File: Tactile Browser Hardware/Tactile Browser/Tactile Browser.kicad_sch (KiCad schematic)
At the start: 79 parts, among them SW1 SW_Push, SW10 SW_Push, SW11 SW_Push, SW12 SW_Push, SW13 SW_Push, SW14 SW_Push, SW15 SW_Push, SW16 SW_Push, SW17 SW_Push, SW18 SW_Push, SW19 SW_Push, SW2 SW_Push, SW20 SW_Push, SW3 SW_Push, SW4 SW_Push, SW5 SW_Push, SW6 SW_Push, SW7 SW_Push, SW8 SW_Push, SW9 SW_Push

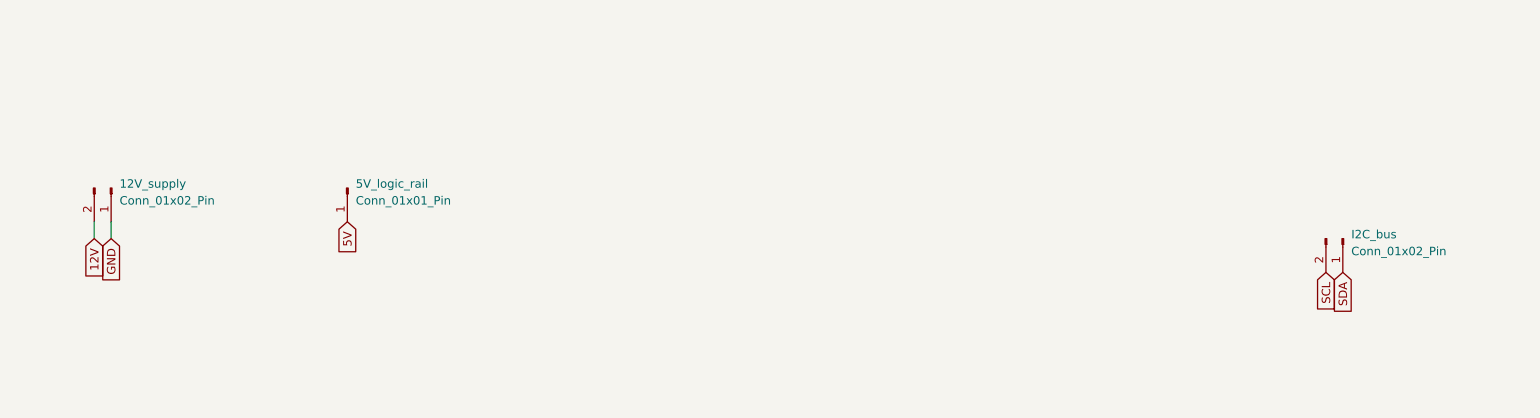
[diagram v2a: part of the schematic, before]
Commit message: added footprints to module
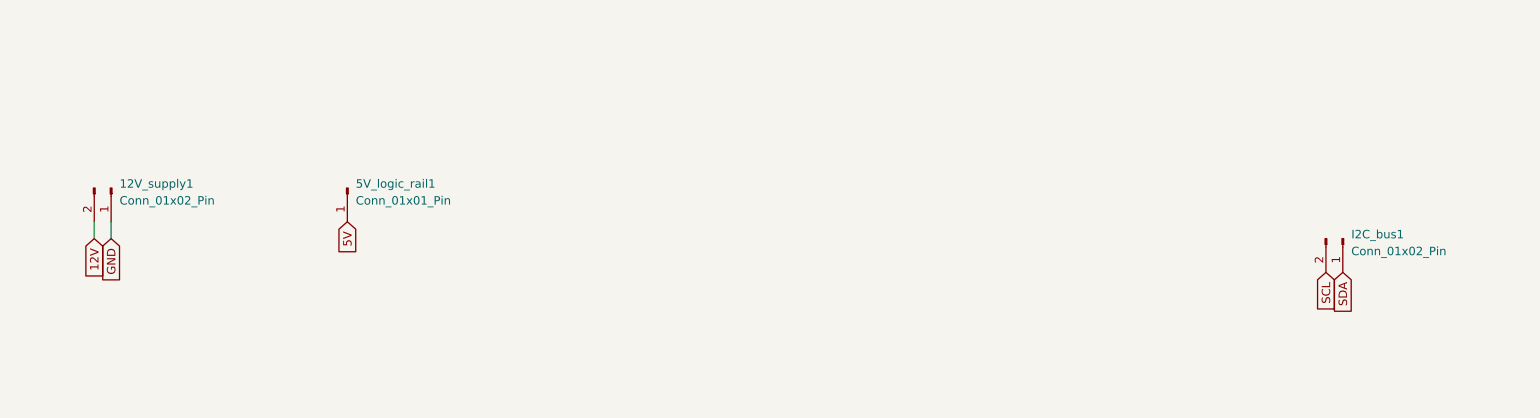
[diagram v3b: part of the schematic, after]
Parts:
- 12V_supply1: renamed from 12V_supply; footprint (none) -> TerminalBlock_Altech:Altech_AK100_1x02_P5.00mm
- 5V_logic_rail1: renamed from 5V_logic_rail; footprint (none) -> TerminalBlock:TerminalBlock_Xinya_XY308-2.54-2P_1x02_P2.54mm_Horizontal
- I2C_bus1: renamed from I2C_bus; footprint (none) -> TerminalBlock:TerminalBlock_Xinya_XY308-2.54-2P_1x02_P2.54mm_Horizontal
- IO_1, IO_2, IO_3, IO_4, IO_5: footprint (none) -> Package_DIP:DIP-16_W7.62mm
- SW1, SW10, SW11, SW12, SW13, SW14, SW15, SW16, SW17, SW18, SW19, SW2, SW20, SW3, SW4, SW5, SW6, SW7, SW8, SW9: footprint (none) -> TerminalBlock:TerminalBlock_Xinya_XY308-2.54-2P_1x02_P2.54mm_Horizontal
- Solenoid1: footprint (none) -> Connector_JST:JST_VH_B2P-VH_1x02_P3.96mm_Vertical
- Solenoid10, Solenoid14, Solenoid2: footprint Connector_Wire:SolderWire-2.5sqmm_1x02_P8.8mm_D2.4mm_OD4.4mm -> Connector_JST:JST_VH_B2P-VH-B_1x02_P3.96mm_Vertical
- Solenoid11, Solenoid12, Solenoid13, Solenoid15, Solenoid16, Solenoid17, Solenoid19, Solenoid20, Solenoid3, Solenoid4, Solenoid5, Solenoid6, Solenoid7, Solenoid8, Solenoid9: footprint (none) -> Connector_JST:JST_VH_B2P-VH-B_1x02_P3.96mm_Vertical
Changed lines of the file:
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@@
 			)
 		)
-		(property "Footprint" ""
+		(property "Footprint" "Connector_JST:JST_VH_B2P-VH-B_1x02_P3.96mm_Vertical"
 			(at 492.76 251.46 0)
 			(effects
@@
 			)
 		)
-		(property "Footprint" ""
+		(property "Footprint" "Connector_JST:JST_VH_B2P-VH-B_1x02_P3.96mm_Vertical"
 			(at 491.49 278.13 0)
 			(effects
@@
 			)
 		)
-		(property "Footprint" ""
+		(property "Footprint" "Connector_JST:JST_VH_B2P-VH-B_1x02_P3.96mm_Vertical"
 			(at 492.76 288.29 0)
 			(effects
@@
 			)
 		)
-		(property "Footprint" ""
+		(property "Footprint" "Connector_JST:JST_VH_B2P-VH-B_1x02_P3.96mm_Vertical"
 			(at 52.07 284.48 0)
 			(effects
@@
 			)
 		)
-		(property "Footprint" ""
+		(property "Footprint" "Package_DIP:DIP-16_W7.62mm"
 			(at 238.76 154.94 0)
 			(effects
@@
 			)
 		)
-		(property "Footprint" ""
+		(property "Footprint" "Connector_JST:JST_VH_B2P-VH-B_1x02_P3.96mm_Vertical"
 			(at 53.34 270.51 0)
 			(effects
@@
 			)
 		)
-		(property "Footprint" ""
+		(property "Footprint" "Connector_JST:JST_VH_B2P-VH-B_1x02_P3.96mm_Vertical"
 			(at 492.76 299.72 0)
 			(effects
@@
 			)
 		)
-		(property "Footprint" ""
+		(property "Footprint" "TerminalBlock:TerminalBlock_Xinya_XY308-2.54-2P_1x02_P2.54mm_Horizontal"
 			(at 487.68 82.55 0)
 			(effects
@@
 			)
 		)
-		(property "Footprint" ""
+		(property "Footprint" "Package_DIP:DIP-16_W7.62mm"
 			(at 283.21 300.99 0)
 			(effects
@@
 			)
 		)
-		(property "Footprint" ""
+		(property "Footprint" "Connector_JST:JST_VH_B2P-VH-B_1x02_P3.96mm_Vertical"
 			(at 53.34 327.66 0)
 			(effects
@@
 			)
 		)
-		(property "Footprint" ""
+		(property "Footprint" "TerminalBlock:TerminalBlock_Xinya_XY308-2.54-2P_1x02_P2.54mm_Horizontal"
 			(at 439.42 44.45 0)
 			(effects
@@
 			)
 		)
-		(property "Footprint" ""
+		(property "Footprint" "Connector_JST:JST_VH_B2P-VH-B_1x02_P3.96mm_Vertical"
 			(at 54.61 259.08 0)
 			(effects
@@
 			)
 		)
-		(property "Footprint" ""
+		(property "Footprint" "TerminalBlock:TerminalBlock_Xinya_XY308-2.54-2P_1x02_P2.54mm_Horizontal"
 			(at 440.69 64.77 0)
 			(effects
@@
 			)
 		)
-		(property "Footprint" ""
+		(property "Footprint" "TerminalBlock:TerminalBlock_Xinya_XY308-2.54-2P_1x02_P2.54mm_Horizontal"
 			(at 463.55 99.06 0)
 			(effects
@@
 			)
 		)
-		(property "Footprint" ""
+		(property "Footprint" "Connector_JST:JST_VH_B2P-VH-B_1x02_P3.96mm_Vertical"
 			(at 53.34 241.3 0)
 			(effects
@@
 			)
 		)
-		(property "Footprint" ""
+		(property "Footprint" "Connector_JST:JST_VH_B2P-VH_1x02_P3.96mm_Vertical"
 			(at 491.49 218.44 0)
 			(effects
@@
 			)
 		)
-		(property "Footprint" "Connector_Wire:SolderWire-2.5sqmm_1x02_P8.8mm_D2.4mm_OD4.4mm"
+		(property "Footprint" "Connector_JST:JST_VH_B2P-VH-B_1x02_P3.96mm_Vertical"
 			(at 53.34 293.37 0)
 			(effects
@@
 			)
 		)
-		(property "Footprint" ""
+		(property "Footprint" "Package_DIP:DIP-16_W7.62mm"
 			(at 262.89 346.71 0)
 			(effects
@@
 			)
 		)
-		(property "Footprint" ""
+		(property "Footprint" "Connector_JST:JST_VH_B2P-VH-B_1x02_P3.96mm_Vertical"
 			(at 54.61 303.53 0)
 			(effects
@@
 			)
 		)
-		(property "Footprint" "Connector_Wire:SolderWire-2.5sqmm_1x02_P8.8mm_D2.4mm_OD4.4mm"
+		(property "Footprint" "Connector_JST:JST_VH_B2P-VH-B_1x02_P3.96mm_Vertical"
 			(at 492.76 228.6 0)
 			(effects
@@
 			)
 		)
-		(property "Footprint" ""
+		(property "Footprint" "TerminalBlock:TerminalBlock_Xinya_XY308-2.54-2P_1x02_P2.54mm_Horizontal"
 			(at 533.4 99.06 0)
 			(effects
@@
 			)
 		)
-		(property "Footprint" ""
+		(property "Footprint" "Connector_JST:JST_VH_B2P-VH-B_1x02_P3.96mm_Vertical"
 			(at 491.49 312.42 0)
 			(effects
@@
 			)
 		)
-		(property "Footprint" ""
+		(property "Footprint" "TerminalBlock:TerminalBlock_Xinya_XY308-2.54-2P_1x02_P2.54mm_Horizontal"
 			(at 533.4 64.77 0)
 			(effects
@@
 		(dnp no)
 		(fields_autoplaced yes)
-		(property "Reference" "12V_supply"
+		(property "Reference" "12V_supply1"
 			(at 72.39 57.7849 90)
 			(effects
@@
 			)
 		)
-		(property "Footprint" ""
+		(property "Footprint" "TerminalBlock_Altech:Altech_AK100_1x02_P5.00mm"
 			(at 71.12 58.42 0)
 			(effects
@@
 			(project ""
 				(path "/2e399075-89ae-469c-893b-1284214b820d"
-					(reference "12V_supply")
+					(reference "12V_supply1")
 					(unit 1)
 				)
@@
 			)
 		)
-		(property "Footprint" ""
+		(property "Footprint" "TerminalBlock:TerminalBlock_Xinya_XY308-2.54-2P_1x02_P2.54mm_Horizontal"
 			(at 510.54 99.06 0)
 			(effects
@@
 			)
 		)
-		(property "Footprint" ""
+		(property "Footprint" "TerminalBlock:TerminalBlock_Xinya_XY308-2.54-2P_1x02_P2.54mm_Horizontal"
 			(at 510.54 64.77 0)
 			(effects
@@
 			)
 		)
-		(property "Footprint" ""
+		(property "Footprint" "Package_DIP:DIP-16_W7.62mm"
 			(at 236.22 300.99 0)
 			(effects
@@
 			)
 		)
-		(property "Footprint" ""
+		(property "Footprint" "TerminalBlock:TerminalBlock_Xinya_XY308-2.54-2P_1x02_P2.54mm_Horizontal"
 			(at 510.54 44.45 0)
 			(effects
@@
 			)
 		)
-		(property "Footprint" ""
+		(property "Footprint" "TerminalBlock:TerminalBlock_Xinya_XY308-2.54-2P_1x02_P2.54mm_Horizontal"
 			(at 463.55 44.45 0)
 			(effects
@@
 			)
 		)
-		(property "Footprint" ""
+		(property "Footprint" "TerminalBlock:TerminalBlock_Xinya_XY308-2.54-2P_1x02_P2.54mm_Horizontal"
 			(at 487.68 44.45 0)
 			(effects
@@
 			)
 		)
-		(property "Footprint" ""
+		(property "Footprint" "TerminalBlock:TerminalBlock_Xinya_XY308-2.54-2P_1x02_P2.54mm_Horizontal"
 			(at 510.54 82.55 0)
 			(effects
@@
 			)
 		)
-		(property "Footprint" "Connector_Wire:SolderWire-2.5sqmm_1x02_P8.8mm_D2.4mm_OD4.4mm"
+		(property "Footprint" "Connector_JST:JST_VH_B2P-VH-B_1x02_P3.96mm_Vertical"
 			(at 492.76 322.58 0)
 			(effects
@@
 			)
 		)
-		(property "Footprint" ""
+		(property "Footprint" "Connector_JST:JST_VH_B2P-VH-B_1x02_P3.96mm_Vertical"
 			(at 53.34 232.41 0)
 			(effects
@@
 			)
 		)
-		(property "Footprint" ""
+		(property "Footprint" "Package_DIP:DIP-16_W7.62mm"
 			(at 285.75 156.21 0)
 			(effects
@@
 			)
 		)
-		(property "Footprint" ""
+		(property "Footprint" "TerminalBlock:TerminalBlock_Xinya_XY308-2.54-2P_1x02_P2.54mm_Horizontal"
 			(at 440.69 82.55 0)
 			(effects
@@
 			)
 		)
-		(property "Footprint" ""
+		(property "Footprint" "Connector_JST:JST_VH_B2P-VH-B_1x02_P3.96mm_Vertical"
 			(at 491.49 266.7 0)
 			(effects
@@
 		(dnp no)
 		(fields_autoplaced yes)
-		(property "Reference" "5V_logic_rail"
+		(property "Reference" "5V_logic_rail1"
 			(at 107.95 57.7849 90)
 			(effects
@@
 			)
 		)
-		(property "Footprint" ""
+		(property "Footprint" "TerminalBlock:TerminalBlock_Xinya_XY308-2.54-2P_1x02_P2.54mm_Horizontal"
 			(at 106.68 58.42 0)
 			(effects
@@
 			(project ""
 				(path "/2e399075-89ae-469c-893b-1284214b820d"
-					(reference "5V_logic_rail")
+					(reference "5V_logic_rail1")
 					(unit 1)
 				)
@@
 			)
 		)
-		(property "Footprint" ""
+		(property "Footprint" "TerminalBlock:TerminalBlock_Xinya_XY308-2.54-2P_1x02_P2.54mm_Horizontal"
 			(at 487.68 99.06 0)
 			(effects
@@
 			)
 		)
-		(property "Footprint" ""
+		(property "Footprint" "TerminalBlock:TerminalBlock_Xinya_XY308-2.54-2P_1x02_P2.54mm_Horizontal"
 			(at 463.55 64.77 0)
 			(effects
@@
 			)
 		)
-		(property "Footprint" ""
+		(property "Footprint" "Connector_JST:JST_VH_B2P-VH-B_1x02_P3.96mm_Vertical"
 			(at 494.03 237.49 0)
 			(effects
@@
 		(dnp no)
 		(fields_autoplaced yes)
-		(property "Reference" "I2C_bus"
+		(property "Reference" "I2C_bus1"
 			(at 257.81 65.4049 90)
 			(effects
@@
 			)
 		)
-		(property "Footprint" ""
+		(property "Footprint" "TerminalBlock:TerminalBlock_Xinya_XY308-2.54-2P_1x02_P2.54mm_Horizontal"
 			(at 256.54 66.04 0)
 			(effects
@@
 			(project ""
 				(path "/2e399075-89ae-469c-893b-1284214b820d"
-					(reference "I2C_bus")
+					(reference "I2C_bus1")
 					(unit 1)
 				)
@@
 			)
 		)
-		(property "Footprint" ""
+		(property "Footprint" "TerminalBlock:TerminalBlock_Xinya_XY308-2.54-2P_1x02_P2.54mm_Horizontal"
 			(at 440.69 99.06 0)
 			(effects
@@
 			)
 		)
-		(property "Footprint" ""
+		(property "Footprint" "TerminalBlock:TerminalBlock_Xinya_XY308-2.54-2P_1x02_P2.54mm_Horizontal"
 			(at 533.4 82.55 0)
 			(effects
@@
 			)
 		)
-		(property "Footprint" ""
+		(property "Footprint" "Connector_JST:JST_VH_B2P-VH-B_1x02_P3.96mm_Vertical"
 			(at 54.61 313.69 0)
 			(effects
@@
 			)
 		)
-		(property "Footprint" ""
+		(property "Footprint" "TerminalBlock:TerminalBlock_Xinya_XY308-2.54-2P_1x02_P2.54mm_Horizontal"
 			(at 487.68 64.77 0)
 			(effects
@@
 			)
 		)
-		(property "Footprint" ""
+		(property "Footprint" "TerminalBlock:TerminalBlock_Xinya_XY308-2.54-2P_1x02_P2.54mm_Horizontal"
 			(at 463.55 82.55 0)
 			(effects
@@
 			)
 		)
-		(property "Footprint" ""
+		(property "Footprint" "TerminalBlock:TerminalBlock_Xinya_XY308-2.54-2P_1x02_P2.54mm_Horizontal"
 			(at 533.4 44.45 0)
 			(effects

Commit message: pcb edits + updated driver footprint
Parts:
- Driver1, Driver10, Driver2, Driver3, Driver4, Driver5, Driver6, Driver7, Driver8, Driver9: footprint Package_SO:SSOP-24_5.3x8.2mm_P0.65mm -> Package_DIP:DIP-24_W15.24mm
- Solenoid18: footprint Connector_Wire:SolderWire-2.5sqmm_1x02_P8.8mm_D2.4mm_OD4.4mm -> Connector_JST:JST_VH_B2P-VH-B_1x02_P3.96mm_Vertical
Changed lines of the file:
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@@
 			)
 		)
-		(property "Footprint" "Connector_Wire:SolderWire-2.5sqmm_1x02_P8.8mm_D2.4mm_OD4.4mm"
+		(property "Footprint" "Connector_JST:JST_VH_B2P-VH-B_1x02_P3.96mm_Vertical"
 			(at 53.34 248.92 0)
 			(effects
@@
 			)
 		)
-		(property "Footprint" "Package_SO:SSOP-24_5.3x8.2mm_P0.65mm"
+		(property "Footprint" "Package_DIP:DIP-24_W15.24mm"
 			(at 457.2 300.99 0)
 			(effects
@@
 			)
 		)
-		(property "Footprint" "Package_SO:SSOP-24_5.3x8.2mm_P0.65mm"
+		(property "Footprint" "Package_DIP:DIP-24_W15.24mm"
 			(at 412.75 381 0)
 			(effects
@@
 			)
 		)
-		(property "Footprint" "Package_SO:SSOP-24_5.3x8.2mm_P0.65mm"
+		(property "Footprint" "Package_DIP:DIP-24_W15.24mm"
 			(at 157.48 299.72 0)
 			(effects
@@
 			)
 		)
-		(property "Footprint" "Package_SO:SSOP-24_5.3x8.2mm_P0.65mm"
+		(property "Footprint" "Package_DIP:DIP-24_W15.24mm"
 			(at 215.9 208.28 0)
 			(effects
@@
 			)
 		)
-		(property "Footprint" "Package_SO:SSOP-24_5.3x8.2mm_P0.65mm"
+		(property "Footprint" "Package_DIP:DIP-24_W15.24mm"
 			(at 453.39 208.28 0)
 			(effects
@@
 			)
 		)
-		(property "Footprint" "Package_SO:SSOP-24_5.3x8.2mm_P0.65mm"
+		(property "Footprint" "Package_DIP:DIP-24_W15.24mm"
 			(at 217.17 297.18 0)
 			(effects
@@
 			)
 		)
-		(property "Footprint" "Package_SO:SSOP-24_5.3x8.2mm_P0.65mm"
+		(property "Footprint" "Package_DIP:DIP-24_W15.24mm"
 			(at 383.54 298.45 0)
 			(effects
@@
 			)
 		)
-		(property "Footprint" "Package_SO:SSOP-24_5.3x8.2mm_P0.65mm"
+		(property "Footprint" "Package_DIP:DIP-24_W15.24mm"
 			(at 190.5 379.73 0)
 			(effects
@@
 			)
 		)
-		(property "Footprint" "Package_SO:SSOP-24_5.3x8.2mm_P0.65mm"
+		(property "Footprint" "Package_DIP:DIP-24_W15.24mm"
 			(at 161.29 205.74 0)
 			(effects
@@
 			)
 		)
-		(property "Footprint" "Package_SO:SSOP-24_5.3x8.2mm_P0.65mm"
+		(property "Footprint" "Package_DIP:DIP-24_W15.24mm"
 			(at 378.46 208.28 0)
 			(effects

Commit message: pcb edits
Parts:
- Driver1, Driver10, Driver2, Driver3, Driver4, Driver5, Driver6, Driver7, Driver8, Driver9: footprint Package_DIP:DIP-24_W15.24mm -> Connector_PinHeader_2.54mm:PinHeader_2x08_P2.54mm_Vertical
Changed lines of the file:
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@@
 			)
 		)
-		(property "Footprint" "Package_DIP:DIP-24_W15.24mm"
+		(property "Footprint" "Connector_PinHeader_2.54mm:PinHeader_2x08_P2.54mm_Vertical"
 			(at 457.2 300.99 0)
 			(effects
@@
 			)
 		)
-		(property "Footprint" "Package_DIP:DIP-24_W15.24mm"
+		(property "Footprint" "Connector_PinHeader_2.54mm:PinHeader_2x08_P2.54mm_Vertical"
 			(at 412.75 381 0)
 			(effects
@@
 			)
 		)
-		(property "Footprint" "Package_DIP:DIP-24_W15.24mm"
+		(property "Footprint" "Connector_PinHeader_2.54mm:PinHeader_2x08_P2.54mm_Vertical"
 			(at 157.48 299.72 0)
 			(effects
@@
 			)
 		)
-		(property "Footprint" "Package_DIP:DIP-24_W15.24mm"
+		(property "Footprint" "Connector_PinHeader_2.54mm:PinHeader_2x08_P2.54mm_Vertical"
 			(at 215.9 208.28 0)
 			(effects
@@
 			)
 		)
-		(property "Footprint" "Package_DIP:DIP-24_W15.24mm"
+		(property "Footprint" "Connector_PinHeader_2.54mm:PinHeader_2x08_P2.54mm_Vertical"
 			(at 453.39 208.28 0)
 			(effects
@@
 			)
 		)
-		(property "Footprint" "Package_DIP:DIP-24_W15.24mm"
+		(property "Footprint" "Connector_PinHeader_2.54mm:PinHeader_2x08_P2.54mm_Vertical"
 			(at 217.17 297.18 0)
 			(effects
@@
 			)
 		)
-		(property "Footprint" "Package_DIP:DIP-24_W15.24mm"
+		(property "Footprint" "Connector_PinHeader_2.54mm:PinHeader_2x08_P2.54mm_Vertical"
 			(at 383.54 298.45 0)
 			(effects
@@
 			)
 		)
-		(property "Footprint" "Package_DIP:DIP-24_W15.24mm"
+		(property "Footprint" "Connector_PinHeader_2.54mm:PinHeader_2x08_P2.54mm_Vertical"
 			(at 190.5 379.73 0)
 			(effects
@@
 			)
 		)
-		(property "Footprint" "Package_DIP:DIP-24_W15.24mm"
+		(property "Footprint" "Connector_PinHeader_2.54mm:PinHeader_2x08_P2.54mm_Vertical"
 			(at 161.29 205.74 0)
 			(effects
@@
 			)
 		)
-		(property "Footprint" "Package_DIP:DIP-24_W15.24mm"
+		(property "Footprint" "Connector_PinHeader_2.54mm:PinHeader_2x08_P2.54mm_Vertical"
 			(at 378.46 208.28 0)
 			(effects

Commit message: update
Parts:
- Driver1, Driver10, Driver2, Driver3, Driver4, Driver5, Driver6, Driver7, Driver8, Driver9: footprint Connector_PinHeader_2.54mm:PinHeader_2x08_P2.54mm_Vertical -> TB6612FNG_THT:TB6612FNG_DualPinHeader_1x8x2_P2.54mm_Row15.24mm_THT
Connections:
- net 12V: no longer Driver1.13 (VM2), Driver1.14 (VM3), Driver10.13 (VM2), Driver10.14 (VM3), Driver2.13 (VM2), Driver2.14 (VM3), Driver3.13 (VM2), Driver3.14 (VM3), Driver4.13 (VM2), Driver4.14 (VM3), Driver5.13 (VM2), Driver5.14 (VM3), Driver6.13 (VM2), Driver6.14 (VM3), Driver7.13 (VM2), Driver7.14 (VM3), Driver8.13 (VM2), Driver8.14 (VM3), Driver9.13 (VM2), Driver9.14 (VM3)
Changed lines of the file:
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@@
 	)
 	(symbol
+		(lib_name "TB6612FNG_3")
 		(lib_id "Driver_Motor:TB6612FNG")
 		(at 424.18 278.13 0)
@@
 			)
 		)
-		(property "Footprint" "Connector_PinHeader_2.54mm:PinHeader_2x08_P2.54mm_Vertical"
+		(property "Footprint" "TB6612FNG_THT:TB6612FNG_DualPinHeader_1x8x2_P2.54mm_Row15.24mm_THT"
 			(at 457.2 300.99 0)
 			(effects
@@
 		(pin "4"
 		)
-		(pin "13"
+		(pin "24"
 		)
-		(pin "14"
+		(pin "24"
 		)
 		(pin "10"
@@
 	)
 	(symbol
+		(lib_name "TB6612FNG_5")
 		(lib_id "Driver_Motor:TB6612FNG")
 		(at 379.73 358.14 0)
@@
 			)
 		)
-		(property "Footprint" "Connector_PinHeader_2.54mm:PinHeader_2x08_P2.54mm_Vertical"
+		(property "Footprint" "TB6612FNG_THT:TB6612FNG_DualPinHeader_1x8x2_P2.54mm_Row15.24mm_THT"
 			(at 412.75 381 0)
 			(effects
@@
 		(pin "4"
 		)
-		(pin "13"
+		(pin "24"
 		)
-		(pin "14"
+		(pin "24"
 		)
 		(pin "10"
@@
 	)
 	(symbol
+		(lib_name "TB6612FNG_8")
 		(lib_id "Driver_Motor:TB6612FNG")
 		(at 124.46 276.86 0)
@@
 			)
 		)
-		(property "Footprint" "Connector_PinHeader_2.54mm:PinHeader_2x08_P2.54mm_Vertical"
+		(property "Footprint" "TB6612FNG_THT:TB6612FNG_DualPinHeader_1x8x2_P2.54mm_Row15.24mm_THT"
 			(at 157.48 299.72 0)
 			(effects
@@
 		(pin "4"
 		)
-		(pin "13"
+		(pin "24"
 		)
-		(pin "14"
+		(pin "24"
 		)
 		(pin "10"
@@
 	)
 	(symbol
+		(lib_name "TB6612FNG_6")
 		(lib_id "Driver_Motor:TB6612FNG")
 		(at 182.88 185.42 0)
@@
 			)
 		)
-		(property "Footprint" "Connector_PinHeader_2.54mm:PinHeader_2x08_P2.54mm_Vertical"
+		(property "Footprint" "TB6612FNG_THT:TB6612FNG_DualPinHeader_1x8x2_P2.54mm_Row15.24mm_THT"
 			(at 215.9 208.28 0)
 			(effects
@@
 		(pin "4"
 		)
-		(pin "13"
+		(pin "24"
 		)
-		(pin "14"
+		(pin "24"
 		)
 		(pin "10"
@@
 	)
 	(symbol
+		(lib_name "TB6612FNG_2")
 		(lib_id "Driver_Motor:TB6612FNG")
 		(at 420.37 185.42 0)
@@
 			)
 		)
-		(property "Footprint" "Connector_PinHeader_2.54mm:PinHeader_2x08_P2.54mm_Vertical"
+		(property "Footprint" "TB6612FNG_THT:TB6612FNG_DualPinHeader_1x8x2_P2.54mm_Row15.24mm_THT"
 			(at 453.39 208.28 0)
 			(effects
@@
 		(pin "4"
 		)
-		(pin "13"
+		(pin "24"
 		)
-		(pin "14"
+		(pin "24"
 		)
 		(pin "10"
@@
 	)
 	(symbol
+		(lib_name "TB6612FNG_9")
 		(lib_id "Driver_Motor:TB6612FNG")
 		(at 184.15 274.32 0)
@@
 			)
 		)
-		(property "Footprint" "Connector_PinHeader_2.54mm:PinHeader_2x08_P2.54mm_Vertical"
+		(property "Footprint" "TB6612FNG_THT:TB6612FNG_DualPinHeader_1x8x2_P2.54mm_Row15.24mm_THT"
 			(at 217.17 297.18 0)
 			(effects
@@
 		(pin "4"
 		)
-		(pin "13"
+		(pin "24"
 		)
-		(pin "14"
+		(pin "24"
 		)
 		(pin "10"
@@
 	)
 	(symbol
+		(lib_name "TB6612FNG_4")
 		(lib_id "Driver_Motor:TB6612FNG")
 		(at 350.52 275.59 0)
@@
 			)
 		)
-		(property "Footprint" "Connector_PinHeader_2.54mm:PinHeader_2x08_P2.54mm_Vertical"
+		(property "Footprint" "TB6612FNG_THT:TB6612FNG_DualPinHeader_1x8x2_P2.54mm_Row15.24mm_THT"
 			(at 383.54 298.45 0)
 			(effects
@@
 		(pin "4"
 		)
-		(pin "13"
+		(pin "24"
 		)
-		(pin "14"
+		(pin "24"
 		)
 		(pin "10"
@@
 			)
 		)
-		(property "Footprint" "Connector_PinHeader_2.54mm:PinHeader_2x08_P2.54mm_Vertical"
+		(property "Footprint" "TB6612FNG_THT:TB6612FNG_DualPinHeader_1x8x2_P2.54mm_Row15.24mm_THT"
 			(at 190.5 379.73 0)
 			(effects
@@
 		(pin "4"
 		)
-		(pin "13"
+		(pin "24"
 		)
-		(pin "14"
+		(pin "24"
 		)
 		(pin "10"
@@
 	)
 	(symbol
+		(lib_name "TB6612FNG_7")
 		(lib_id "Driver_Motor:TB6612FNG")
 		(at 128.27 182.88 0)
@@
 			)
 		)
-		(property "Footprint" "Connector_PinHeader_2.54mm:PinHeader_2x08_P2.54mm_Vertical"
+		(property "Footprint" "TB6612FNG_THT:TB6612FNG_DualPinHeader_1x8x2_P2.54mm_Row15.24mm_THT"
 			(at 161.29 205.74 0)
 			(effects
@@
 		(pin "4"
 		)
-		(pin "13"
+		(pin "24"
 		)
-		(pin "14"
+		(pin "24"
 		)
 		(pin "10"
@@
 	)
 	(symbol
+		(lib_name "TB6612FNG_1")
 		(lib_id "Driver_Motor:TB6612FNG")
 		(at 345.44 185.42 0)
@@
 			)
 		)
-		(property "Footprint" "Connector_PinHeader_2.54mm:PinHeader_2x08_P2.54mm_Vertical"
+		(property "Footprint" "TB6612FNG_THT:TB6612FNG_DualPinHeader_1x8x2_P2.54mm_Row15.24mm_THT"
 			(at 378.46 208.28 0)
 			(effects
@@
 		(pin "4"
 		)
-		(pin "13"
+		(pin "24"
 		)
-		(pin "14"
+		(pin "24"
 		)
 		(pin "10"
